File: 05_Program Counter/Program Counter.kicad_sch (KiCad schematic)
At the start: 9 parts, among them J1 Data Out 1, J2 Data Out 2, J3 Address Out 1, J4 Address Out 2, J5 Data bus, J6 Address Bus 1, J7 Address Bus 2, J8 Input 1, J9 Input 2

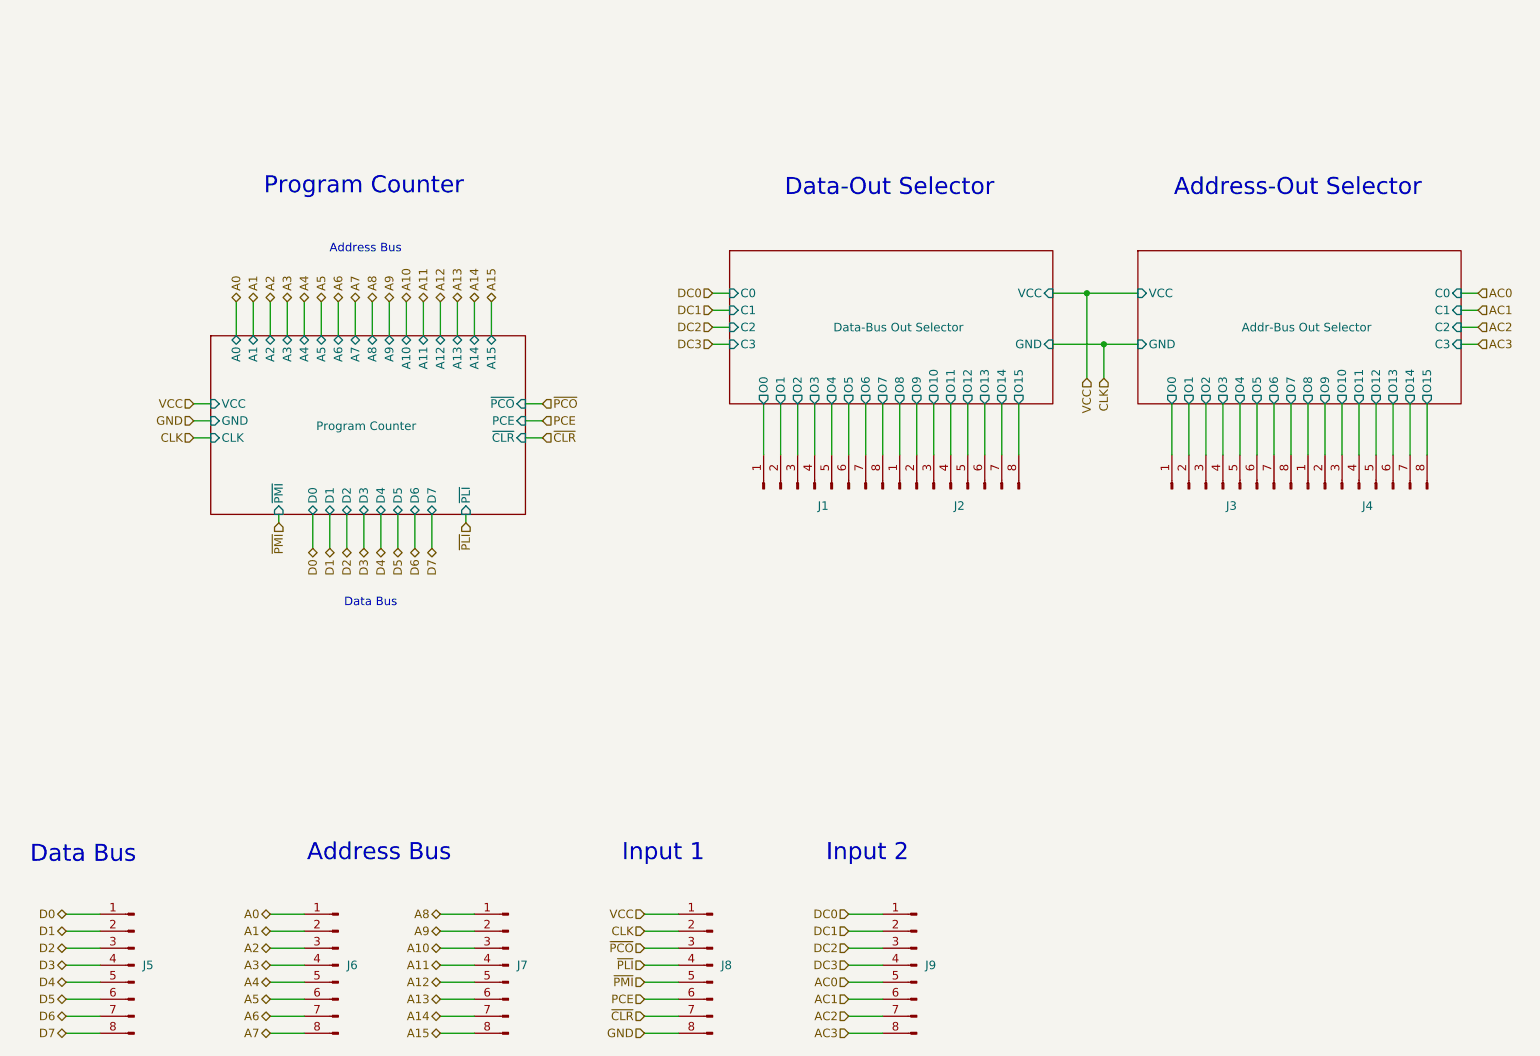
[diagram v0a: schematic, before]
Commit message: Last revision of the cpu, all boards have been ordered. Implementation to be tested and documented in following commits.
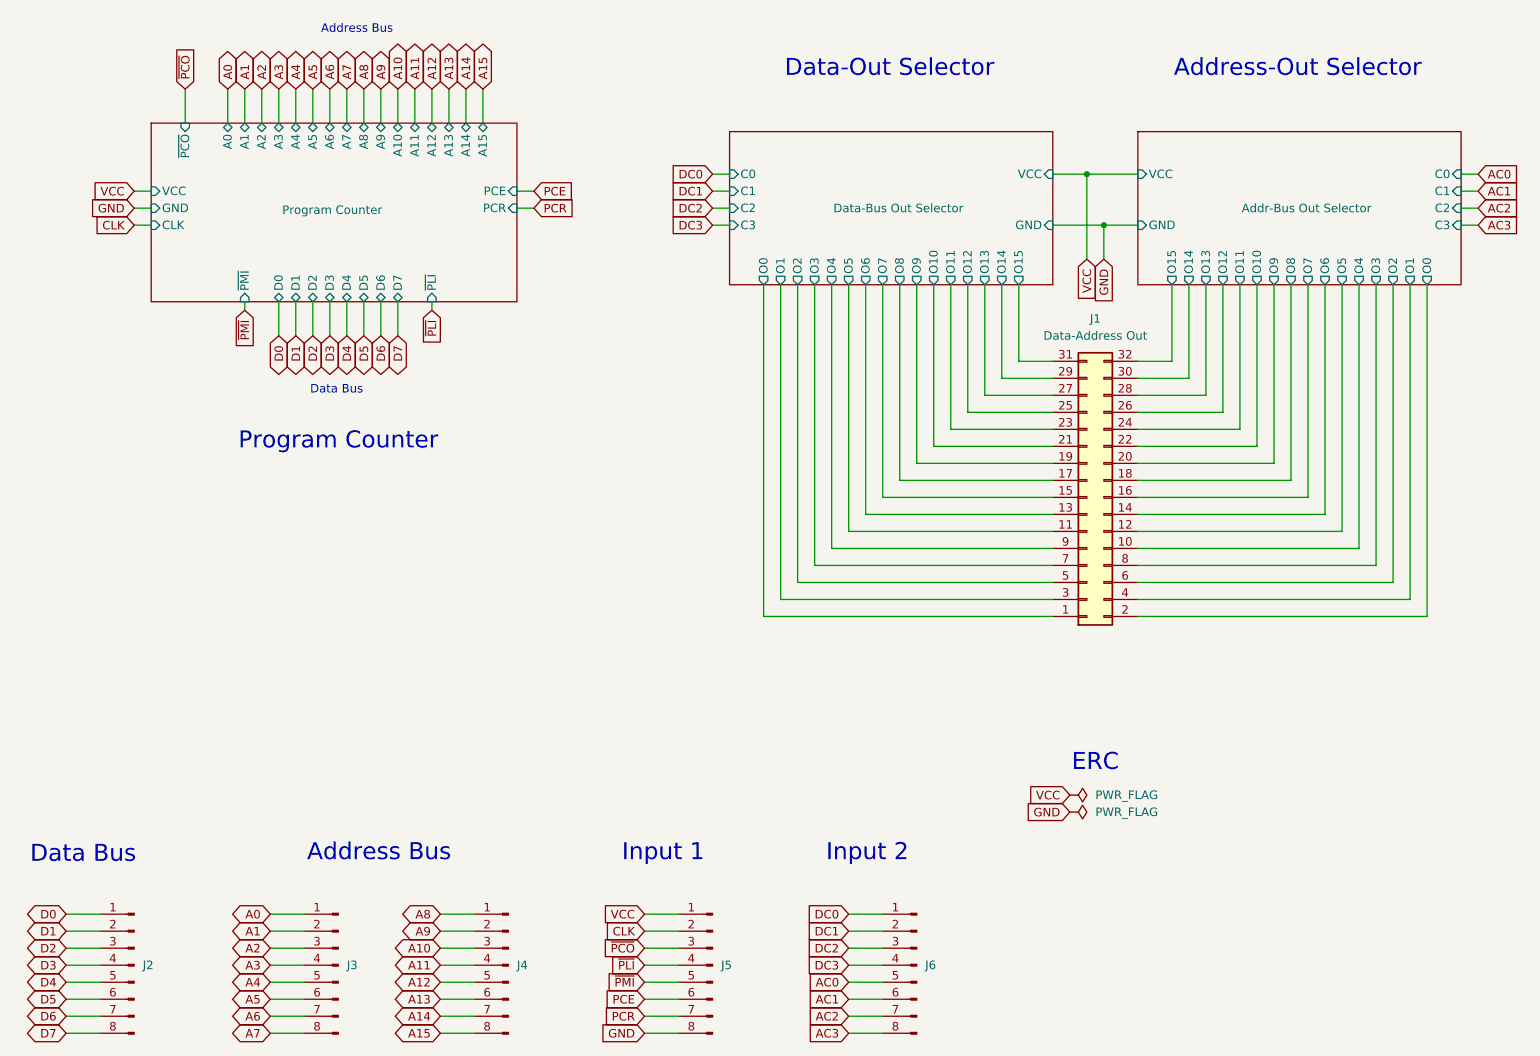
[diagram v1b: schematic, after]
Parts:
- removed J1: Data Out 1, Custom:PinHeader_1x08_P2.54mm_Vertical, symbol Connector:Conn_01x08_Pin
- removed J2: Data Out 2, Custom:PinHeader_1x08_P2.54mm_Vertical, symbol Connector:Conn_01x08_Pin
- removed J3: Address Out 1, Custom:PinHeader_1x08_P2.54mm_Vertical, symbol Connector:Conn_01x08_Pin
- removed J4: Address Out 2, Custom:PinHeader_1x08_P2.54mm_Vertical, symbol Connector:Conn_01x08_Pin
- added J1: Data-Address Out, Connector_PinHeader_2.54mm:PinHeader_2x16_P2.54mm_Horizontal, symbol Connector_Generic:Conn_02x16_Odd_Even
- renumbered J5 to J2, J6 to J3, J7 to J4, J8 to J5, J9 to J6
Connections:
- net Addr-Bus Out Selector/O0: now also J1.2 (Pin_2)
- net Addr-Bus Out Selector/O1: now also J1.4 (Pin_4)
- net Addr-Bus Out Selector/O10: now also J1.22 (Pin_22)
- net Addr-Bus Out Selector/O11: now also J1.24 (Pin_24)
- net Addr-Bus Out Selector/O12: now also J1.26 (Pin_26)
- net Addr-Bus Out Selector/O13: now also J1.28 (Pin_28)
- net Addr-Bus Out Selector/O14: now also J1.30 (Pin_30)
- net Addr-Bus Out Selector/O15: now also J1.32 (Pin_32)
- net Addr-Bus Out Selector/O2: now also J1.6 (Pin_6)
- net Addr-Bus Out Selector/O3: now also J1.8 (Pin_8)
- net Addr-Bus Out Selector/O4: now also J1.10 (Pin_10)
- net Addr-Bus Out Selector/O5: now also J1.12 (Pin_12)
- net Addr-Bus Out Selector/O6: now also J1.14 (Pin_14)
- net Addr-Bus Out Selector/O7: now also J1.16 (Pin_16)
- net Addr-Bus Out Selector/O8: now also J1.18 (Pin_18)
- net Addr-Bus Out Selector/O9: now also J1.20 (Pin_20)
- net Data-Bus Out Selector/O0: now also J1.1 (Pin_1)
- net Data-Bus Out Selector/O1: now also J1.3 (Pin_3)
- net Data-Bus Out Selector/O10: now also J1.21 (Pin_21)
- net Data-Bus Out Selector/O11: now also J1.23 (Pin_23)
- net Data-Bus Out Selector/O12: now also J1.25 (Pin_25)
- net Data-Bus Out Selector/O13: now also J1.27 (Pin_27)
- net Data-Bus Out Selector/O14: now also J1.29 (Pin_29)
- net Data-Bus Out Selector/O15: now also J1.31 (Pin_31)
- net Data-Bus Out Selector/O2: now also J1.5 (Pin_5)
- net Data-Bus Out Selector/O3: now also J1.7 (Pin_7)
- net Data-Bus Out Selector/O4: now also J1.9 (Pin_9)
- net Data-Bus Out Selector/O5: now also J1.11 (Pin_11)
- net Data-Bus Out Selector/O6: now also J1.13 (Pin_13)
- net Data-Bus Out Selector/O7: now also J1.15 (Pin_15)
- net Data-Bus Out Selector/O8: now also J1.17 (Pin_17)
- net Data-Bus Out Selector/O9: now also J1.19 (Pin_19)
- net ~{CLR} renamed PCR
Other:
- sheet Program Counter ports: added PCR; removed ~{CLR}
- note added: "ERC"
